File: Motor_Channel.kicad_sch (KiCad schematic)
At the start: 30 parts, among them J301 MOTOR_OUT, Q301 CSD18540Q5B, Q302 CSD18540Q5B, Q303 CSD18540Q5B, Q304 CSD18540Q5B, U301 DRV8701ERGER

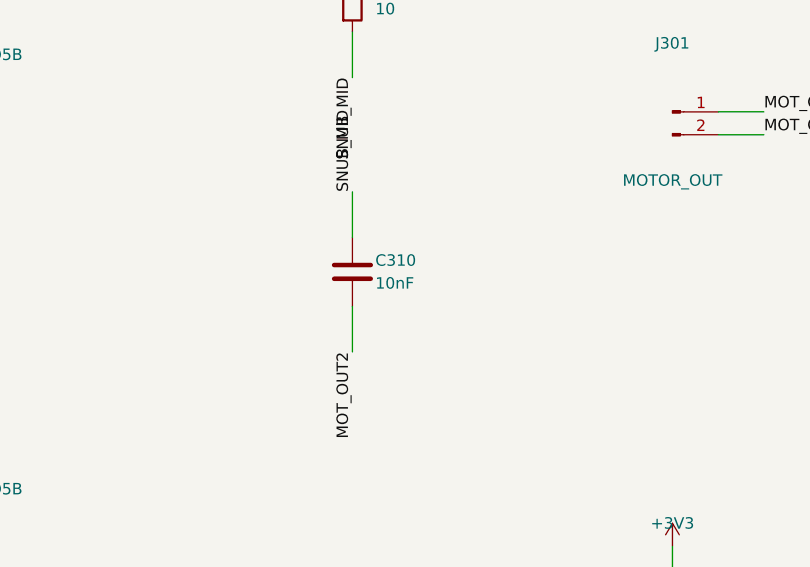
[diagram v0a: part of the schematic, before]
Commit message: Resolve all 5 prototype review items (F1 3557-2 4-pad THT, SMCJ30A, 2.2nF/0.5W snubber, 0.45-0.50mm stepper traces, clean PTH/NPTH drills)
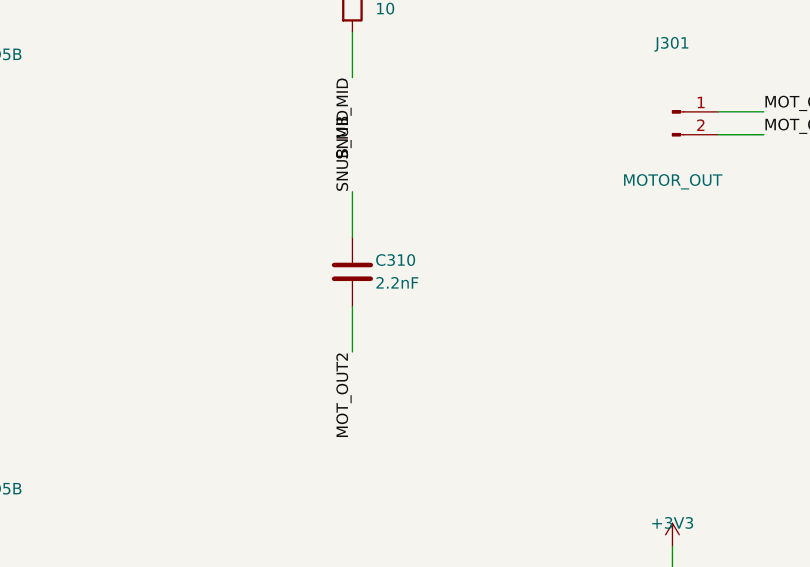
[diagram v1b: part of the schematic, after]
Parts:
- C310: value 10nF -> 2.2nF
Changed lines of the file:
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@@
 			)
 		)
-		(property "Value" "10nF"
+		(property "Value" "2.2nF"
 			(at 345.44 87.63 0)
 			(effects

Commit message: Release v1.0-production: finalize F1 3D STEP model alignment and archive V1.0 production package
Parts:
- removed R312: 200k, Resistor_SMD:R_0603_1608Metric, symbol Device:R
- C310: value 2.2nF -> 10nF
- R309: value 10mR_3W -> 10m
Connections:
- net DRV_IDRIVE is gone; now on net GND: U301.12 (IDRIVE)
- net PWM_EN: now also U301.15 (EN); no longer U301.14 (EN)
- net PWM_PH: now also U301.14 (PH); no longer U301.15 (PH)

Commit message: Complete V1.1 compact 6-channel I/O & DC output architecture (0 ERC, 0 DRC errors, 0 unconnected, 0 parity)
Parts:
- added R312: 200k, Resistor_SMD:R_0603_1608Metric, symbol Device:R
- C310: value 10nF -> 2.2nF
- R309: value 10m -> 10mR_3W
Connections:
- net GND: now also R312.2; no longer U301.12 (IDRIVE)
- net PWM_EN: now also U301.14 (EN); no longer U301.15 (EN)
- net PWM_PH: now also U301.15 (PH); no longer U301.14 (PH)
- new net DRV_IDRIVE: R312.1, U301.12 (IDRIVE)

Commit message: Finalize Rev 1.1d robustness, thermal layout and manufacturing package
Preserve sensing and current-limit fixes, assembly part/rotation corrections,
D2 package changes, revision markings and incremental thermal copper/vias.
Archive the working checkpoints and supplier/validation evidence alongside
matched Gerbers, BOM, CPL, schematic PDF, renders and hash manifests.

Current Rev 1.1d: ERC 0; DRC 0 errors, 0 opens and 0 parity issues,
with 19 existing library footprint warnings. Preserve original routing and
component placements; physical powered qualification is not yet performed.
Relay alignment requires assembler review before assembly.
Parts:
- added R313: 1k, Resistor_SMD:R_0603_1608Metric, symbol Device:R
- R302: value 30k -> 12k
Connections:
- net CS: now also R313.1
- net GND: now also R313.2
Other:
- note added: "ADC protection: R304/R404 + R313/R413 divide SO by 2; rescale firmware."
- title: (none) -> ABX-Motion
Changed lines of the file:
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@@
 	(generator_version "10.0")
 	(paper "A3")
+	(title_block (title "ABX-Motion") (rev "1.1d"))
 	(text "SHEET 3: 100W BRUSHED DC SERVO CHANNEL (DRV8701ERGER + 4x CSD18540Q5B 60V H-BRIDGE)"
 		(exclude_from_sim no)
@@
 			)
 		)
-		(property "Value" "30k"
+		(property "Value" "12k"
 			(at 144.78 166.37 0)
 			(effects
@@
 	)
 	(embedded_fonts no)
+	(text "ADC protection: R304/R404 + R313/R413 divide SO by 2; rescale firmware."
+		(exclude_from_sim no)
+		(at 193.04 187.96 0)
+		(effects
+			(font
+				(size 1.27 1.27)
+				(bold yes)
+			)
+			(justify left bottom)
+		)
+	)
+	(wire
+		(pts
+			(xy 254 171.45) (xy 254 166.37)
+		)
+		(stroke
+			(width 0)
+			(type default)
+		)
+	)
+	(wire
+		(pts
+			(xy 254 179.07) (xy 254 182.88)
+		)
+		(stroke
+			(width 0)
+			(type default)
+		)
+	)
+	(label "CS"
+		(at 254 166.37 90)
+		(fields_autoplaced yes)
+		(effects
+			(font
+				(size 1.27 1.27)
+			)
+			(justify left bottom)
+		)
+	)
+	(symbol
+		(lib_id "Device:R")
+		(at 254 175.26 0)
+		(unit 1)
+		(exclude_from_sim no)
+		(in_bom yes)
+		(on_board yes)
+		(dnp no)
+		(fields_autoplaced yes)
+		(property "Reference" "R313"
+			(at 256.54 173.99 0)
+			(effects
+				(font
+					(size 1.27 1.27)
+				)
+				(justify left)
+				(hide no)
+			)
+		)
+		(property "Value" "1k"
+			(at 256.54 176.53 0)
+			(effects
+				(font
+					(size 1.27 1.27)
+				)
+				(justify left)
+			)
+		)
+		(property "Footprint" "Resistor_SMD:R_0603_1608Metric"
+			(at 254 175.26 0)
+			(effects
+				(font
+					(size 1.27 1.27)
+				)
+				(hide yes)
+			)
+		)
+		(property "Datasheet" "~"
+			(at 254 175.26 0)
+			(effects
+				(font
+					(size 1.27 1.27)
+				)
+				(hide yes)
+			)
+		)
+		(pin "1"
+		)
+		(pin "2"
+		)
+		(instances
+			(project "abx-motion"
+				(path "/f9149098-3f23-438d-bdc2-2e278b5ca35b/92b8d963-008c-44ee-80dc-a4ddc2493923"
+					(reference "R313")
+					(unit 1)
+				)
+				(path "/f9149098-3f23-438d-bdc2-2e278b5ca35b/40d2ba13-688c-4a36-ae2b-0996c3aab01d"
+					(reference "R413")
+					(unit 1)
+				)
+			)
+		)
+	)
+	(symbol
+		(lib_id "power:GND")
+		(at 254 182.88 0)
+		(unit 1)
+		(exclude_from_sim no)
+		(in_bom yes)
+		(on_board yes)
+		(dnp no)
+		(fields_autoplaced yes)
+		(property "Reference" "#PWR9000"
+			(at 254 186.69 0)
+			(effects
+				(font
+					(size 1.27 1.27)
+				)
+				(hide yes)
+			)
+		)
+		(property "Value" "GND"
+			(at 254 185.42 0)
+			(effects
+				(font
+					(size 1.27 1.27)
+				)
+			)
+		)
+		(property "Footprint" ""
+			(at 254 182.88 0)
+			(effects
+				(font
+					(size 1.27 1.27)
+				)
+				(hide yes)
+			)
+		)
+		(property "Datasheet" "~"
+			(at 254 182.88 0)
+			(effects
+				(font
+					(size 1.27 1.27)
+				)
+				(hide yes)
+			)
+		)
+		(pin "1"
+		)
+		(instances
+			(project "abx-motion"
+				(path "/f9149098-3f23-438d-bdc2-2e278b5ca35b/92b8d963-008c-44ee-80dc-a4ddc2493923"
+					(reference "#PWR9000")
+					(unit 1)
+				)
+				(path "/f9149098-3f23-438d-bdc2-2e278b5ca35b/40d2ba13-688c-4a36-ae2b-0996c3aab01d"
+					(reference "#PWR9500")
+					(unit 1)
+				)
+			)
+		)
+	)
 )

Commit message: Save Rev 1.2a three-axis checkpoint and audited JLCPCB exports
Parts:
- C301, C303, C304: LCSC (none) -> C15849
- C302, C309: LCSC (none) -> C14663
- C305: LCSC (none) -> C57112
- C306: LCSC (none) -> C72499
- C307, C308: LCSC (none) -> C29823
- C310: LCSC (none) -> C107136
- J301: LCSC (none) -> C8465
- LED_FLT1: LCSC (none) -> C2286
- Q301, Q302, Q303, Q304: LCSC (none) -> C86513
- R301: LCSC (none) -> C25810
- R302: LCSC (none) -> C22790
- R303: LCSC (none) -> C25804
- R304, R311, R313: LCSC (none) -> C21190
- R305, R306, R307, R308: LCSC (none) -> C22859
- R309: LCSC (none) -> C840621
- R310: LCSC (none) -> C844598
- R312: LCSC (none) -> C25811
- U301: LCSC (none) -> C90964

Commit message: Clear root project DRC findings and preserve explicit Ethernet draft status
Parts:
- J301: footprint TerminalBlock_Phoenix:TerminalBlock_Phoenix_MKDS-1,5-2-5.08_1x02_P5.08mm_Horizontal -> abx-footprints:MKDS_2Pin_Motor_ABX
- TP_CS1: footprint TestPoint:TestPoint_Pad_D1.5mm -> abx-footprints:TestPoint_PTH_2.5x3.6_D1.0_CS_ABX
- U301: footprint Package_DFN_QFN:Texas_RGE0024C_VQFN-24-1EP_4x4mm_P0.5mm_EP2.1x2.1mm_ThermalVias -> abx-footprints:DRV8701_RGE_Thermal_ABX
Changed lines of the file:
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@@
 			)
 		)
-		(property "Footprint" "Package_DFN_QFN:Texas_RGE0024C_VQFN-24-1EP_4x4mm_P0.5mm_EP2.1x2.1mm_ThermalVias"
+		(property "Footprint" "abx-footprints:DRV8701_RGE_Thermal_ABX"
 			(at 76.2 78.74 0)
 			(effects
@@
 			)
 		)
-		(property "Footprint" "TestPoint:TestPoint_Pad_D1.5mm"
+		(property "Footprint" "abx-footprints:TestPoint_PTH_2.5x3.6_D1.0_CS_ABX"
 			(at 228.6 124.46 0)
 			(effects
@@
 			)
 		)
-		(property "Footprint" "TerminalBlock_Phoenix:TerminalBlock_Phoenix_MKDS-1,5-2-5.08_1x02_P5.08mm_Horizontal"
+		(property "Footprint" "abx-footprints:MKDS_2Pin_Motor_ABX"
 			(at 378.46 68.58 0)
 			(effects
